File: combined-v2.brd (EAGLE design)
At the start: 128.3 x 142.2 mm, 385 parts, among them IC2 PCM1865DBT, U11 TMUX1204DGSR, U2 LM4562MAX/NOPB, U3 TMUX1204DGSR, U4 TMUX1204DGSR, U5 TMUX1204DGSR, Y2 ECS-245.7-20-3X-EN-TR

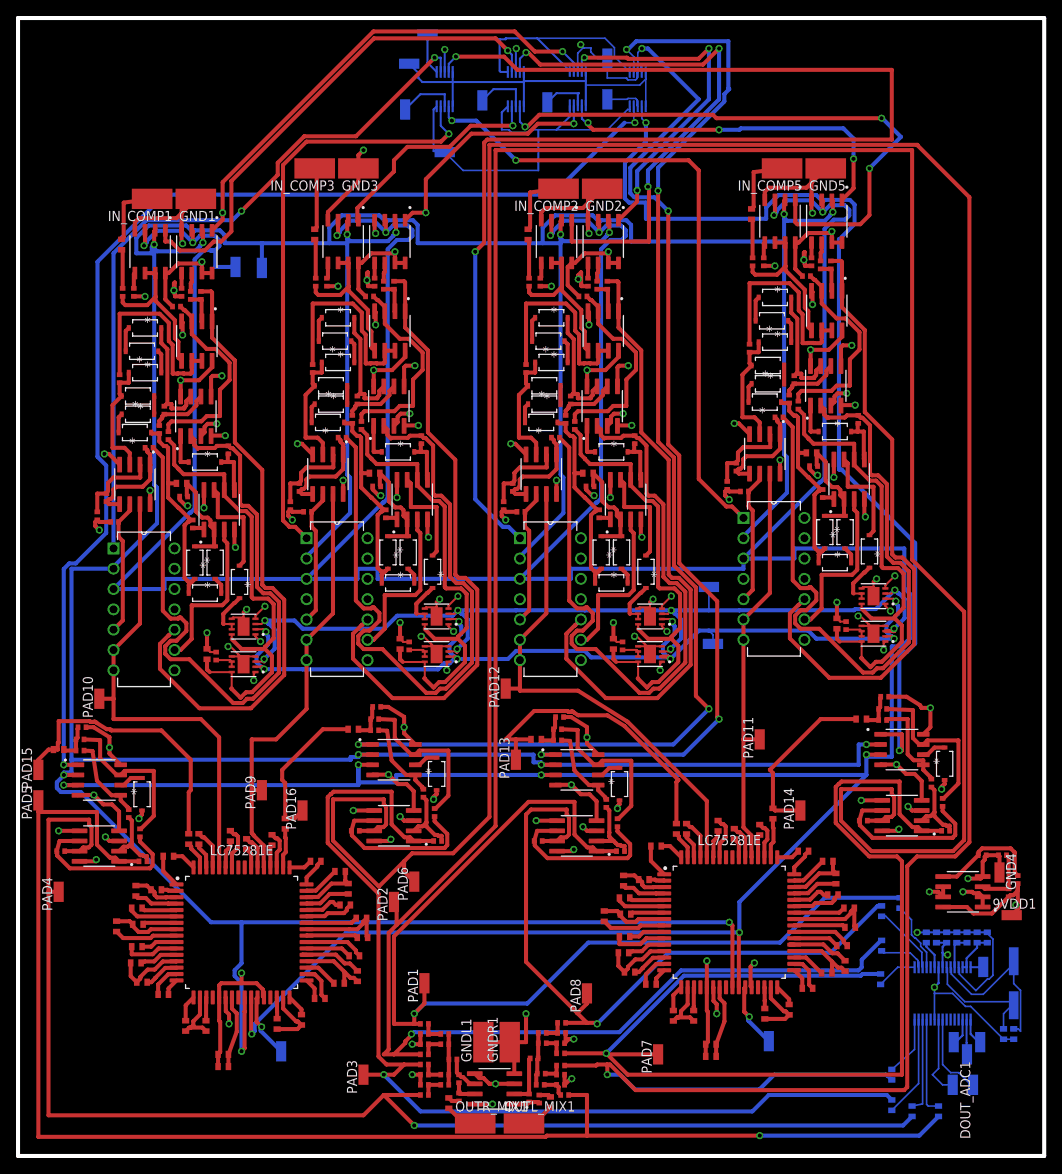
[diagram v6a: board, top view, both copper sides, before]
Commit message: replace incorrect diode size
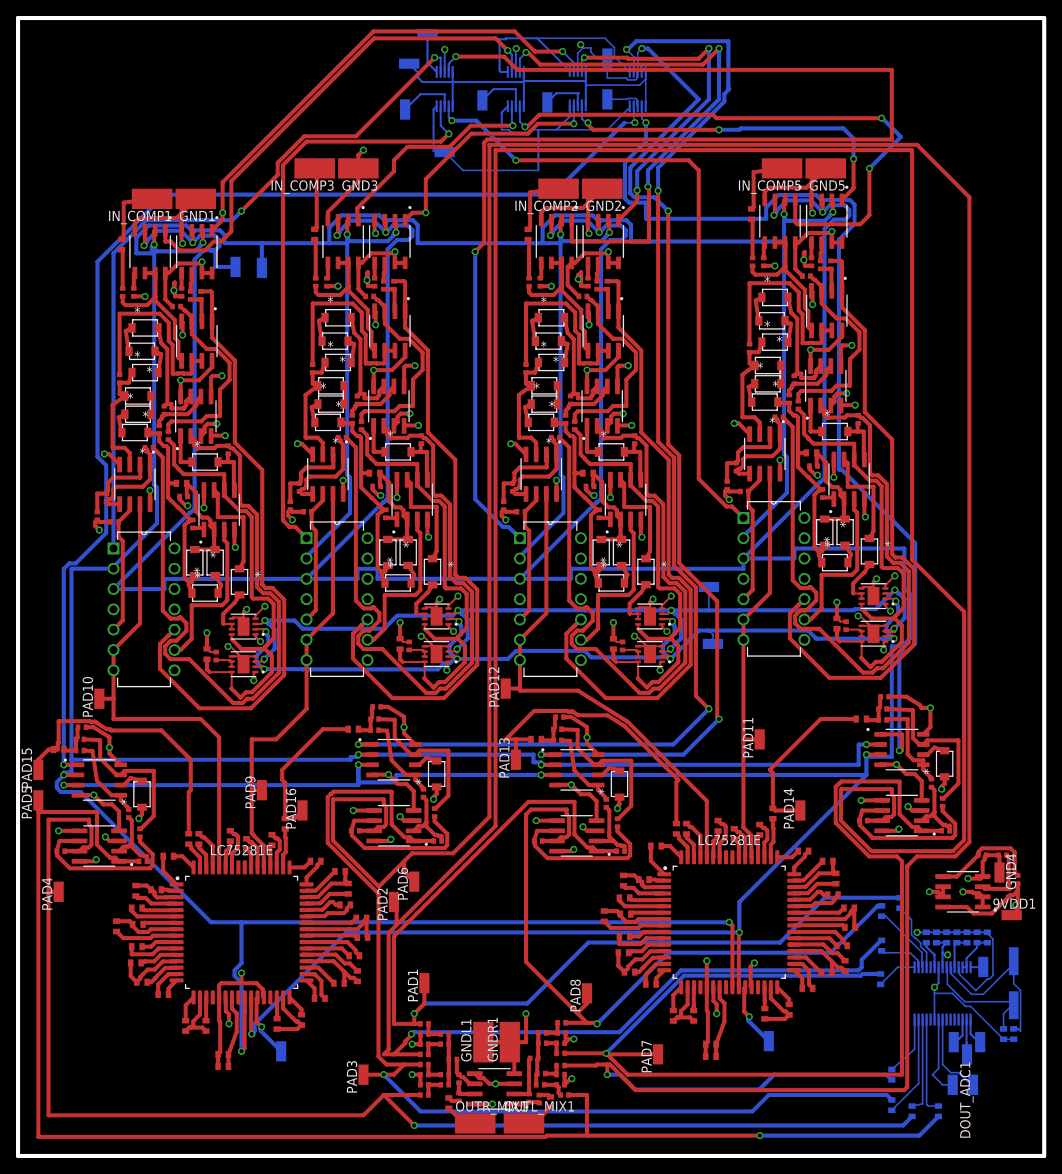
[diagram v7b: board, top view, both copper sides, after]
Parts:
- D16, D17, D18, D19, D2, D20, D21, D22, D23, D24, D25, D26, D27, D28, D29, D3, D30, D31, D32, D33, D34, D35, D36, D37, D38, D39, D4, D40, D41, D42, D43, D44, D45, D46, D47, D48, D5, D60, D61, D62, D63, D64, D65, D66, D67, D68, D69, D70: device 1N4148W-TP:SOD123 -> 1N4148W-TP(1):SOD123
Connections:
- net L1_COMP1: now also D19.1; no longer D19.C
- net L1_COMP2: now also D41.1; no longer D41.C
- net L1_COMP3: now also D30.1; no longer D30.C
- net L1_COMP4: now also D63.1; no longer D63.C
- net N$100: now also D64.2, D65.1; no longer D64.A, D65.C
- net N$102: now also D68.2, D69.1; no longer D68.A, D69.C
- net N$103: now also D67.2, D68.1; no longer D67.A, D68.C
- net N$211: now also D17.2, D18.1, D25.2; no longer D17.A, D18.C, D25.A
- net N$212: now also D39.2, D40.1, D47.2; no longer D39.A, D40.C, D47.A
- net N$213: now also D28.2, D29.1, D36.2; no longer D28.A, D29.C, D36.A
- net N$214: now also D61.2, D62.1, D69.2; no longer D61.A, D62.C, D69.A
- net N$74: now also D16.2, D17.1; no longer D16.A, D17.C
- net N$75: now also D21.2, D22.1; no longer D21.A, D22.C
- net N$76: now also D20.2, D21.1; no longer D20.A, D21.C
- net N$78: now also D24.2, D25.1; no longer D24.A, D25.C
- net N$79: now also D23.2, D24.1; no longer D23.A, D24.C
- net N$80: now also D27.2, D28.1; no longer D27.A, D28.C
- net N$81: now also D32.2, D33.1; no longer D32.A, D33.C
- net N$82: now also D31.2, D32.1; no longer D31.A, D32.C
- net N$84: now also D35.2, D36.1; no longer D35.A, D36.C
- net N$85: now also D34.2, D35.1; no longer D34.A, D35.C
- net N$86: now also D38.2, D39.1; no longer D38.A, D39.C
- net N$87: now also D43.2, D44.1; no longer D43.A, D44.C
- net N$88: now also D42.2, D43.1; no longer D42.A, D43.C
- net N$90: now also D46.2, D47.1; no longer D46.A, D47.C
- net N$91: now also D45.2, D46.1; no longer D45.A, D46.C
- net N$98: now also D60.2, D61.1; no longer D60.A, D61.C
- net N$99: now also D65.2, D66.1; no longer D65.A, D66.C
- net NEG_A1_COMP1: now also D16.1, D18.2; no longer D16.C, D18.A
- net NEG_A1_COMP2: now also D38.1, D40.2; no longer D38.C, D40.A
- net NEG_A1_COMP3: now also D27.1, D29.2; no longer D27.C, D29.A
- net NEG_A1_COMP4: now also D60.1, D62.2; no longer D60.C, D62.A
- net OUT_A3_COMP1: now also D26.2; no longer D26.A
- net OUT_A3_COMP2: now also D48.2; no longer D48.A
- net OUT_A3_COMP3: now also D37.2; no longer D37.A
- net OUT_A3_COMP4: now also D70.2; no longer D70.A
- net OUT_B1_COMP1: now also D19.2; no longer D19.A
- net OUT_B1_COMP2: now also D41.2; no longer D41.A
- net OUT_B1_COMP3: now also D30.2; no longer D30.A
- net OUT_B1_COMP4: now also D63.2; no longer D63.A
- net OUT_B3_COMP1: now also D20.1; no longer D20.C
- net OUT_B3_COMP2: now also D42.1; no longer D42.C
- net OUT_B3_COMP3: now also D31.1; no longer D31.C
- net OUT_B3_COMP4: now also D64.1; no longer D64.C
- net P0W_PAN1: now also D2.1; no longer D2.C
- net P0W_PAN2: now also D4.1; no longer D4.C
- net P0W_PAN3: now also D3.1; no longer D3.C
- net P0W_PAN4: now also D5.1; no longer D5.C
- net POS_A4_COMP1: now also D22.2, D23.1; no longer D22.A, D23.C
- net POS_A4_COMP2: now also D44.2, D45.1; no longer D44.A, D45.C
- net POS_A4_COMP3: now also D33.2, D34.1; no longer D33.A, D34.C
- net POS_A4_COMP4: now also D66.2, D67.1; no longer D66.A, D67.C
- net POS_B1_COMP1: now also D26.1; no longer D26.C
- net POS_B1_COMP2: now also D48.1; no longer D48.C
- net POS_B1_COMP3: now also D37.1; no longer D37.C
- net POS_B1_COMP4: now also D70.1; no longer D70.C
- net VREF: now also D2.2, D3.2, D4.2, D5.2; no longer D2.A, D3.A, D4.A, D5.A
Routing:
- net VREF: track 1082.2 -> 1083.8 mm
- net N$212: track 26.3 -> 27.4 mm
- net N$211: track 26.3 -> 27.4 mm
- net N$213: track 26.3 -> 27.4 mm
- net N$214: track 26.3 -> 27.4 mm
- net POS_A4_COMP2: track 15.0 -> 15.7 mm
- net POS_A4_COMP3: track 15.0 -> 15.7 mm
- net POS_A4_COMP4: track 15.0 -> 15.7 mm
- net POS_A4_COMP1: track 15.0 -> 15.7 mm
